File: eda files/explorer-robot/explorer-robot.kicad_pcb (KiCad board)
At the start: 4 copper layers, 90 x 90 mm, 177 parts, among them J1 DBG, J10 EXP.DATA, J11 PANEL.BUS, J12 PANEL.CTRL, J13 RF.FRONT, J14 RF.REAR, J2 MAL, J3 MBR, J4 BAT, J5 LED, J7 LID, J8 AI.CAM, J9 EXP.PWR, Q1 Q_PMOS_GSD, SW1 SW_Push, U1 RP2354B, U10 TPS22917DBV, U11 TPS22917DBV, U2 AMS1117-3.3, U3 ICM-20948, U4 TXB0108PW, U5 AMS1117-1.8, U6 TB6612FNG, U7 TPS5430DDA, U8 TPS22917DBV, U9 TPS22917DBV, Y1 ABM8-272-T3

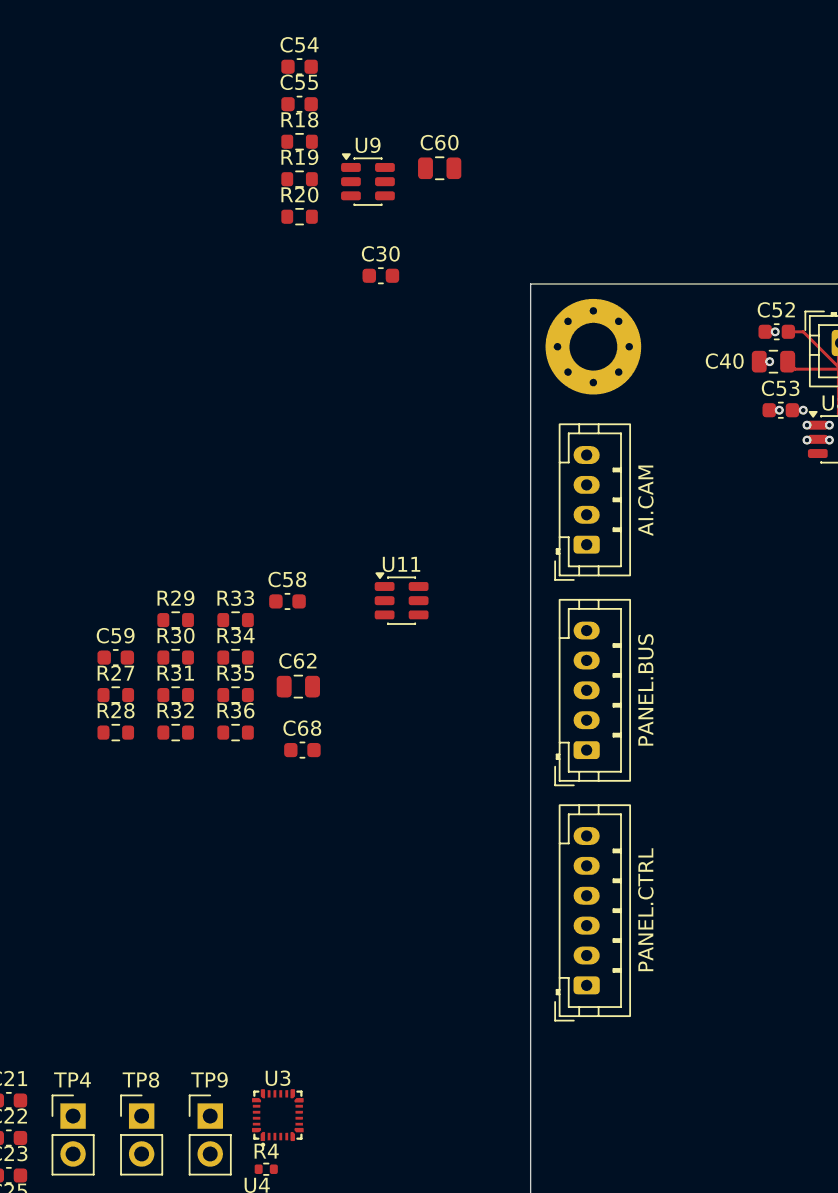
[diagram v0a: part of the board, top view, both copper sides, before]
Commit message: Move power components to robot board edge
Relocate load switch, decoupling caps, and resistors near the
connector edge to shorten high-current paths.
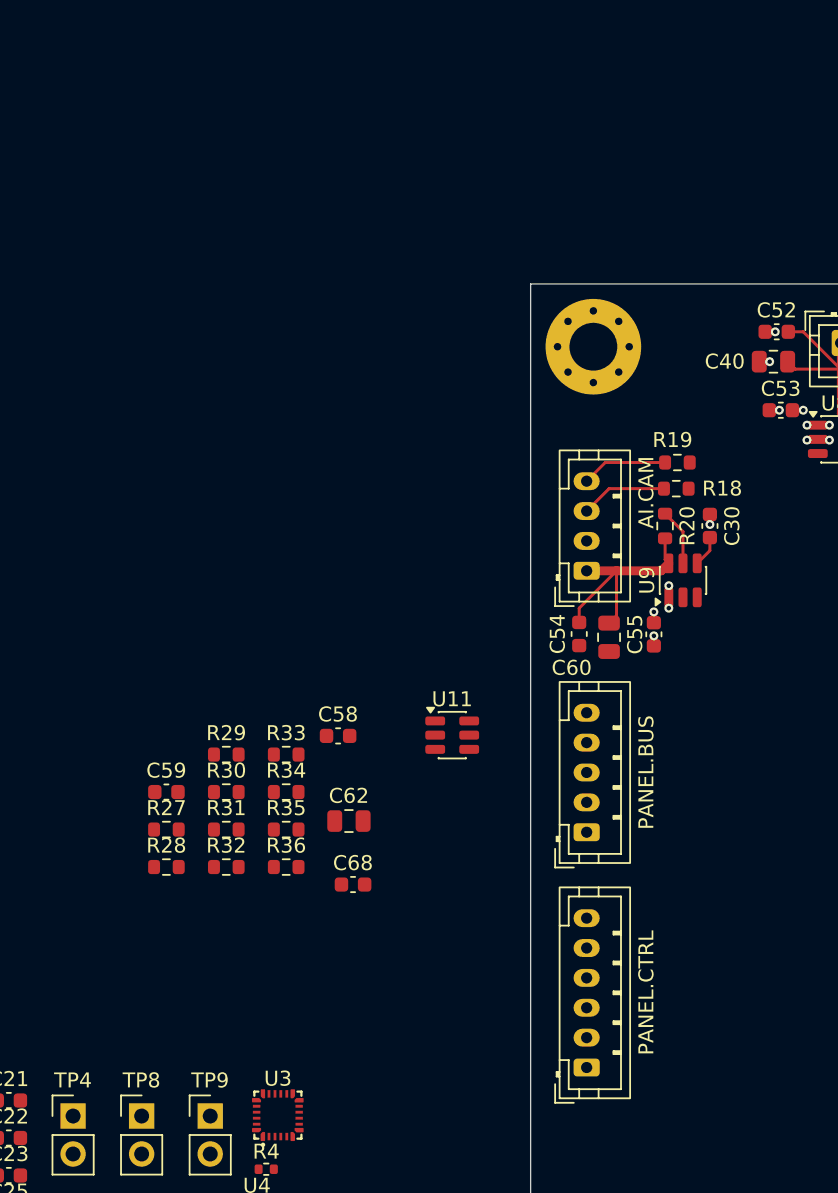
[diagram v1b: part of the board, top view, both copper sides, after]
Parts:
- moved C55 42.7 mm to (106.2, 70.2), turned to 90 degrees
- moved C54 42.3 mm to (101.2, 70.2), turned to 90 degrees
- moved R18 34.3 mm to (107.8, 60.5), turned to 180 degrees
- moved U9 34.0 mm to (108.2, 66.6), turned to 90 degrees
- moved C60 33.4 mm to (103.2, 70.5), turned to -90 degrees
- moved R20 32.1 mm to (107.0, 63.0), turned to 90 degrees
- moved R19 31.6 mm to (107.8, 58.8), turned to 180 degrees
- moved C30 27.7 mm to (110.0, 63.0), turned to 90 degrees
- moved C58 9.62 mm to (85.1, 77.0)
- moved C59 9.62 mm to (73.6, 80.8)
- moved C62 9.62 mm to (85.8, 82.8)
- moved C68 9.62 mm to (86.1, 87.0)
- moved R27 9.62 mm to (73.6, 83.3)
- moved R28 9.62 mm to (73.6, 85.8)
- moved R29 9.62 mm to (77.6, 78.3)
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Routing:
- net Net-(J8-Pin_1): track 0.00 -> 15.7 mm
- net Net-(J8-Pin_3): track 0.00 -> 5.80 mm
- net Net-(J8-Pin_4): track 0.00 -> 5.77 mm
- net Net-(U9-QOD): track 0.00 -> 3.82 mm
- net +5V: track 41.6 -> 44.5 mm, vias 13 -> 17
- net Net-(U9-CT): track 0.00 -> 2.08 mm
- net GND: track 72.9 -> 73.6 mm, vias 51 -> 52

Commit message: connect Panel connectors with passives and switches
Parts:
- moved R30 37.0 mm to (107.9, 102.0)
- moved R28 35.0 mm to (107.2, 76.2), turned to -90 degrees
- moved R31 34.6 mm to (107.9, 100.0)
- moved R27 33.8 mm to (107.2, 79.6), turned to -90 degrees
- moved R32 32.7 mm to (107.9, 98.0)
- moved R36 31.9 mm to (111.0, 73.2), turned to 90 degrees
- moved R33 31.7 mm to (107.9, 96.0)
- moved R29 30.7 mm to (108.0, 73.8)
- moved C68 30.4 mm to (113.2, 73.3), turned to 90 degrees
- moved R34 29.4 mm to (107.9, 94.0)
- moved C59 28.9 mm to (101.8, 87.5), turned to -90 degrees
- moved R35 27.7 mm to (107.9, 92.0)
- moved C58 25.7 mm to (110.5, 80.8), turned to -90 degrees
- moved C62 18.6 mm to (103.8, 87.7), turned to -90 degrees
- moved U11 18.6 mm to (111.3, 76.9), turned to 90 degrees
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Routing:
- net Net-(J11-Pin_1): track 0.00 -> 22.1 mm, vias 0 -> 1
- net Net-(J11-Pin_4): track 0.00 -> 6.39 mm
- net Net-(J11-Pin_5): track 0.00 -> 6.15 mm
- net Net-(J11-Pin_3): track 0.00 -> 5.81 mm
- net Net-(J12-Pin_6): track 0.00 -> 5.35 mm
- net Net-(J12-Pin_5): track 0.00 -> 5.35 mm
- net Net-(J12-Pin_4): track 0.00 -> 5.35 mm
- net Net-(J12-Pin_3): track 0.00 -> 5.35 mm
- net Net-(J12-Pin_2): track 0.00 -> 5.35 mm
- net Net-(J12-Pin_1): track 0.00 -> 5.35 mm
- net +5V: track 44.5 -> 49.5 mm, vias 17 -> 22
- net GND: track 73.6 -> 78.5 mm, vias 52 -> 58
- net Net-(U11-QOD): track 0.00 -> 3.76 mm
- net Net-(U11-CT): track 0.00 -> 2.11 mm

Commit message: panel test points
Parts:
- moved TP26 122.3 mm to (117.8, 147.0), turned to 180 degrees
- moved TP17 121.8 mm to (122.0, 67.0)
- moved TP18 113.3 mm to (118.0, 67.0)
- moved TP19 104.7 mm to (114.0, 67.0)
- moved TP16 81.6 mm to (90.0, 107.8)
- moved TP15 80.2 mm to (89.8, 95.0)
- moved TP14 77.5 mm to (83.5, 91.2)
- moved TP20 68.6 mm to (116.8, 87.5), turned to -90 degrees
- moved TP21 63.6 mm to (116.8, 91.2), turned to -90 degrees
- moved TP27 63.3 mm to (62.0, 67.5)
- moved TP29 62.7 mm to (72.2, 78.5)
- moved TP28 60.5 mm to (65.5, 80.8)
- moved TP22 57.9 mm to (116.8, 95.0), turned to -90 degrees
- moved TP23 27.1 mm to (41.2, 75.5)
- moved TP4 10.00 mm to (67.2, 92.5)
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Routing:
- net /Panel/SPI1_SCK: track 0.00 -> 19.5 mm, vias 0 -> 1
- net /Panel/SPI1_MOSI: track 0.00 -> 14.9 mm, vias 0 -> 1
- net /Panel/LCD_CS: track 0.00 -> 9.27 mm, vias 0 -> 1
- net /Panel/TOUCH_PENIRQ: track 0.00 -> 7.35 mm
- net /Panel/SPI1_MISO: track 0.00 -> 7.06 mm
- net /Panel/TOUCH_CS: track 0.00 -> 6.62 mm

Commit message: route icm-20948
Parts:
- moved TP8 195.1 mm to (268.8, 99.0)
- moved TP9 192.9 mm to (264.0, 109.7)
- moved C61 139.7 mm to (161.2, 31.7)
- moved R24 139.7 mm to (157.0, 30.9)
- moved C56 139.7 mm to (157.0, 18.4)
- moved C57 139.7 mm to (157.0, 20.9)
- moved R21 139.7 mm to (157.0, 23.4)
- moved R22 139.7 mm to (157.0, 25.9)
- moved R23 139.7 mm to (157.0, 28.4)
- moved R25 139.7 mm to (157.0, 33.4)
- moved R26 139.7 mm to (157.0, 35.9)
- moved U10 136.8 mm to (162.9, 24.2)
- moved R45 131.5 mm to (170.9, 127.2), turned to 90 degrees
- moved U5 131.0 mm to (176.2, 128.5)
- moved C67 127.4 mm to (147.4, 34.2)
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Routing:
- net +1V8: track 0.00 -> 60.8 mm, vias 0 -> 2
- net GND: track 78.5 -> 101.5 mm, vias 58 -> 79
- net Net-(U3-~{CS}): track 0.00 -> 21.8 mm, vias 0 -> 2
- net Net-(U3-SCL/SCLK): track 0.00 -> 19.1 mm, vias 0 -> 2
- net /ICM-20948/ICM-20948_CS: track 0.00 -> 13.3 mm
- net Net-(U3-SDA/SDI): track 0.00 -> 11.8 mm, vias 0 -> 2
- net /ICM-20948/ICM-20948_INT: track 0.00 -> 10.7 mm, vias 0 -> 1
- net +3.3V: track 28.1 -> 36.8 mm, vias 15 -> 23
- net /ICM-20948/ICM-20948_SCLK: track 0.00 -> 8.39 mm
- net /ICM-20948/ICM-20948_SDO: track 0.00 -> 7.02 mm
- net Net-(U3-REGOUT): track 0.00 -> 6.82 mm, vias 0 -> 2
- net Net-(U3-SDO/AD0): track 0.00 -> 5.06 mm, vias 0 -> 2
- net Net-(U3-INT1): track 0.00 -> 4.85 mm, vias 0 -> 2
- net /ICM-20948/ICM-20948_SDI: track 0.00 -> 4.21 mm
- net Net-(U4-OE): track 0.00 -> 1.24 mm
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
